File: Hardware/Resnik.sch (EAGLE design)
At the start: 172 parts, among them IC1 ATMEGA644M, J1 CONN_82.54_SCREW, J3 CONN_82.54_SCREW, J4 CONN_42.54_SCREW, Q1 DMG3404, Q2 DMG3404, Q3 FDN360P, Q4 FDN360P, Q5 FDN360P, Q6 DMG3404, U1 TLV61220DBV, U10 SN74AUP1G04YFP, U11 SN74AUP2G86SOT833-1, U12 SN74AUP2G08DQE, U13 SN74AUP2G08DQE, U14 SN74AUP2G08DQE, U15 MIC2039MT, U16 MIC2039MT, U17 MIC2039MT, U18 MIC2039MT, U19 TPS22917DBV, U2 TPS62822DLC, U20 TPS22917DBV, U21 TXS0102DQM, U22 BME280, U23 FT231X-Q, U24 TPS22917DBV, U25 TXS0108RGY, U26 TXS0108RGY, U27 TXS0104RGY, U28 MCP4726A2SOT-23, U29 ADS1115, U3 TPS61032RSA, U30 ADS1115, U31 INA211DCK, U32 INA210DCK, U33 TCA9555RTW, U5 BQ2980RUG, U6 TPS2105, U7 LTC4412S6, U8 TPS79733, U9 SN74AUP1G04YFP

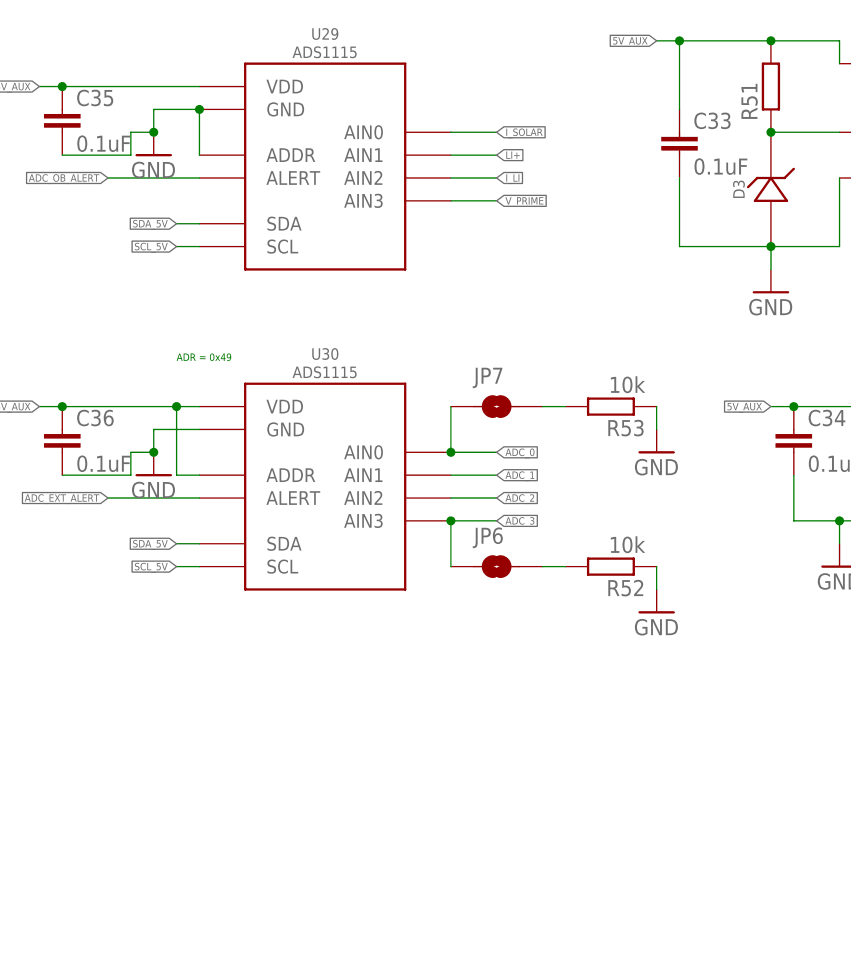
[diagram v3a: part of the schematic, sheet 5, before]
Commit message: Continued layout, major of power and prime bus done
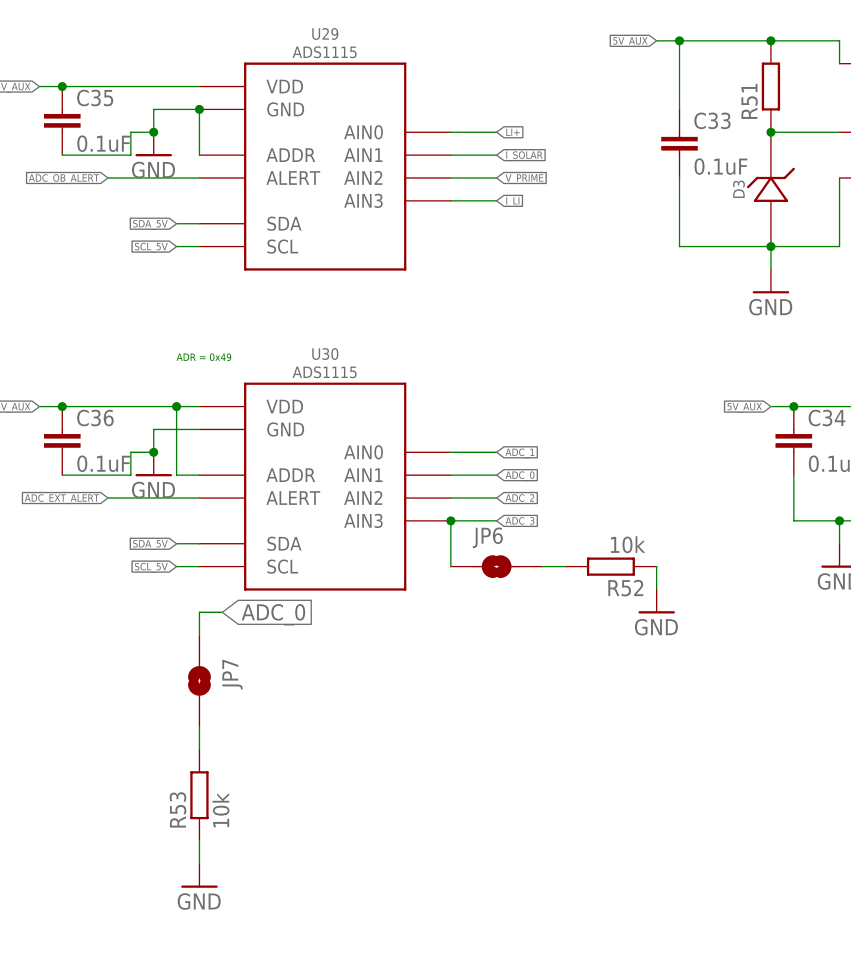
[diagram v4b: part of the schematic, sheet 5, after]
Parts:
- removed R22: 10k, bschulz_passives:R-EU_10KR0402
- added C37, C38, C39: (no value), bschulz_passives:C-EUC0402
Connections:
- net VBAT+ renamed V_CORE
- removed net 3V3: C25.1, IC1.AREF, IC1.AVCC, IC1.VCC, IC1.VCC@1, IC1.VCC@2, ISP2.VCC, R44.2, U$16.ANODE
- new net N$1: IC1.(PCINT2/ADC2)PA2
- net 3V3_AUX: now also C37.1, C38.1, C39.1
- net 3V3_CORE: now also C25.1, IC1.AREF, IC1.AVCC, IC1.VCC, IC1.VCC@1, IC1.VCC@2, ISP2.VCC, R44.2, U$16.ANODE; no longer R22.2
- net ADC_0: now also U30.AIN1; no longer U30.AIN0
- net ADC_1: now also U30.AIN0; no longer U30.AIN1
- net ADC_EXT_ALERT: now also U33.P7
- net BMS_CTR: now also U33.P1
- net BUS_LOGIC_EN_PRIME: now also U33.P6
- net FAULT_PRIME: now also U33.P5
- net GND: now also C37.2, C38.2, C39.2
- net GPIO_1: now also IC1.(PCINT1/ADC1)PA1
- net I_LI: now also U29.AIN3; no longer U29.AIN2
- net I_SOLAR: now also U29.AIN1; no longer U29.AIN0
- net LI+: now also U29.AIN0; no longer U29.AIN1
- net MPPT_CHRG: now also U33.P3
- net MPPT_FAULT: now also U33.P4
- net MPPT_SHDN: now also U33.P2
- net PG_LDO: no longer R22.1
- net SDA: no longer U21.A1
- net SDA_OB: now also U21.A1
- net VUSB_POWER: now also U33.P0
- net V_PRIME: now also U29.AIN2; no longer U29.AIN3
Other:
- note added: "ADD: --MPPT, CHRG (Input) --MPPT, FAULT (Input) --MPPT, SHDN (Output) Feather PowerOn (Output) ADC, OnBoard, Alert/RDY (Input, Interrupt) ADC, OffBoard, Alert/RDY (Input, Interrupt) --Vusb (Input) LevelShifter, Primary Bus, EN (Output) LevelShifter, Secondary Bus, EN (Output) --BMS, CTR (Output) BusPowerSwitch, Primary Bus, Fault (Input) BusPowerSwitch, Secondary Bus, Fault (Input) HighPowerBoost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"
- note removed: "ADD: MPPT, CHRG (Input) MPPT, FAULT (Input) MPPT, SHDN (Output) Feather PowerOn (Output) ADC, OnBoard, Alert/RDY (Input, Interrupt) ADC, OffBoard, Alert/RDY (Input, Interrupt) Vusb (Input) LevelShifter, Primary Bus, EN (Output) LevelShifter, Secondary Bus, EN (Output) BMS, CTR (Output) BusPowerSwitch, Primary Bus, Fault (Input) BusPowerSwitch, Secondary Bus, Fault (Input) HighPowerBoost, LBO (Inp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"
- moved on the sheet: JP7, R53

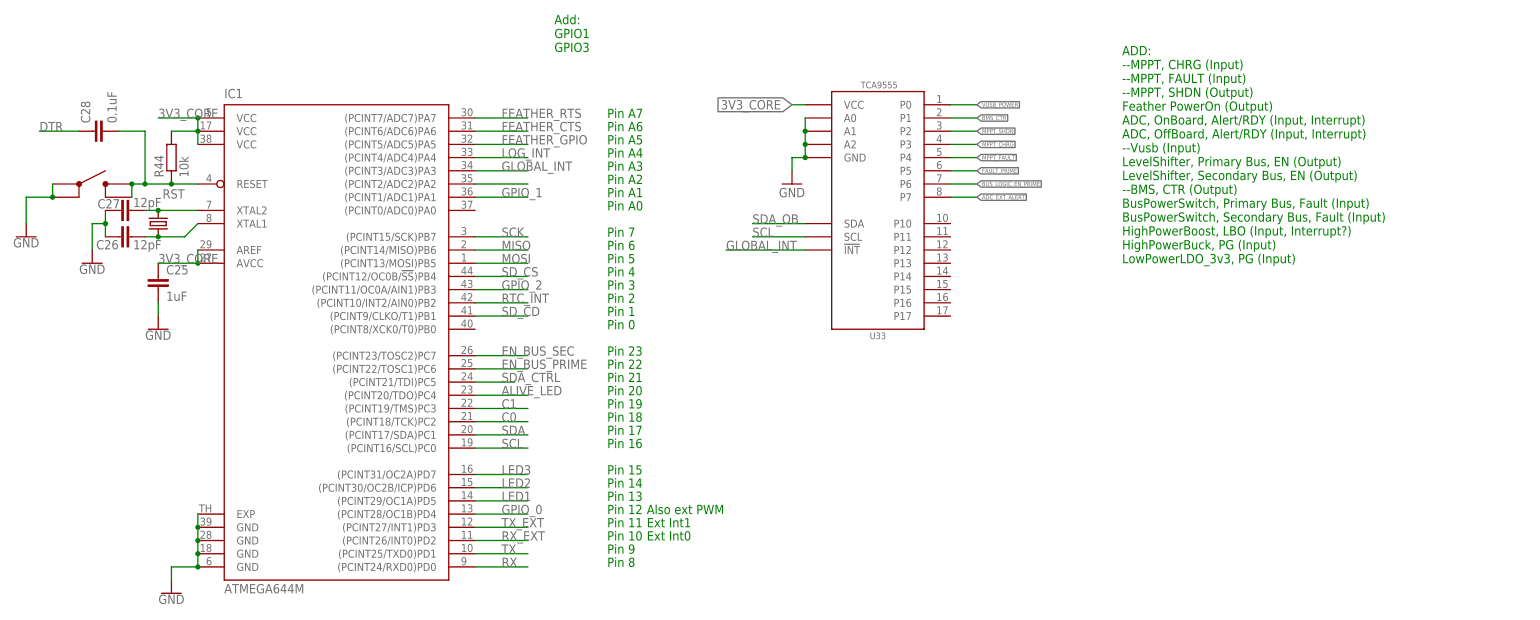
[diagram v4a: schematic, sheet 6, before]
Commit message: Continued layout, majority of secondary bus, low power
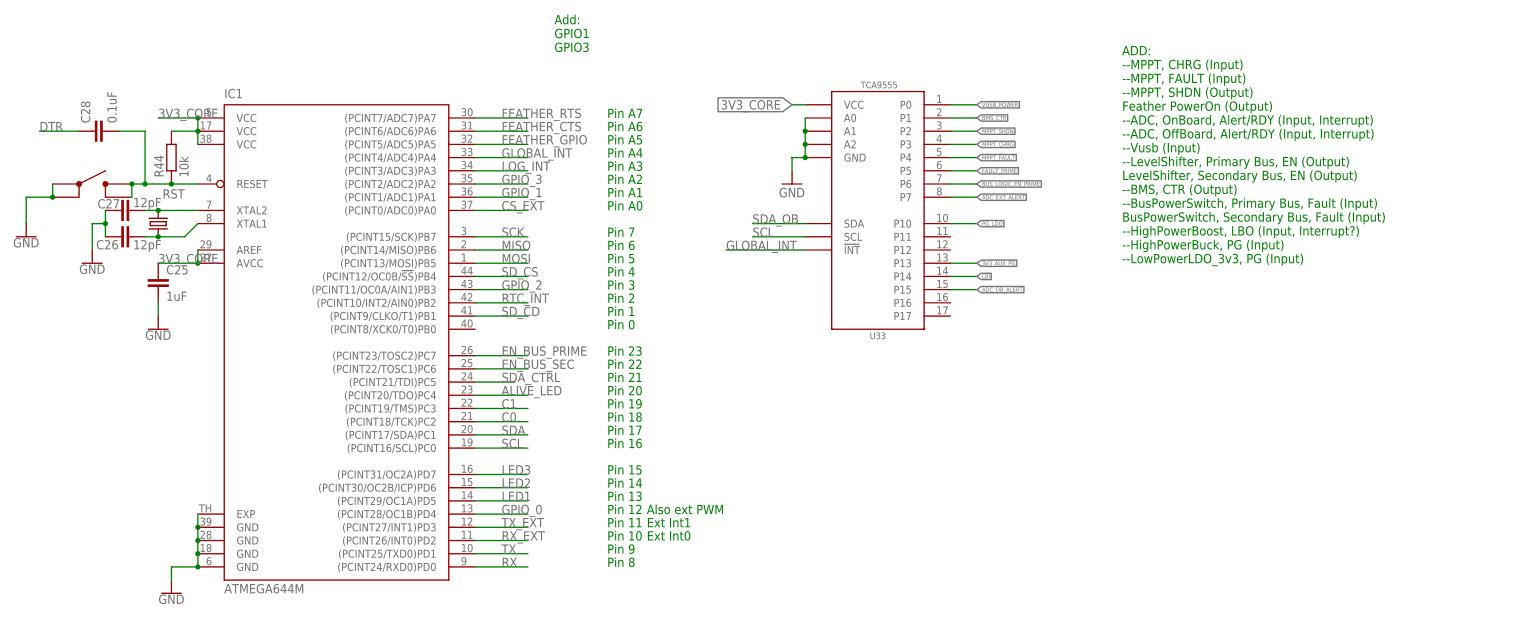
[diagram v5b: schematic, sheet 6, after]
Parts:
- added C40: (no value), bschulz_passives:C-EU0.1UFC0402
- added H1, H2, H3: (no value), bschulz:MOUNTING_HOLE4_NP
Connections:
- removed net N$1: IC1.(PCINT2/ADC2)PA2
- new net FAULT_SEC: U15.!FAULT, U16.!FAULT
- net 3V3_AUX_PG: now also U33.P13
- net ADC_OB_ALERT: now also U33.P15
- net CS_EXT: now also IC1.(PCINT0/ADC0)PA0
- net EN_BUS_PRIME: now also IC1.(PCINT23/TOSC2)PC7; no longer IC1.(PCINT22/TOSC1)PC6
- net EN_BUS_SEC: now also IC1.(PCINT22/TOSC1)PC6; no longer IC1.(PCINT23/TOSC2)PC7
- net FAULT_PRIME: no longer U15.!FAULT, U16.!FAULT
- net GLOBAL_INT: now also IC1.(PCINT4/ADC4)PA4; no longer IC1.(PCINT3/ADC3)PA3
- net GND: now also C40.2
- net GPIO_3: now also IC1.(PCINT2/ADC2)PA2
- net LBI: now also U33.P14
- net LOG_INT: now also IC1.(PCINT3/ADC3)PA3; no longer IC1.(PCINT4/ADC4)PA4
- net N$43: now also C40.1
- net PG_LDO: now also U33.P10
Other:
- note added: "ADD: --MPPT, CHRG (Input) --MPPT, FAULT (Input) --MPPT, SHDN (Output) Feather PowerOn (Output) --ADC, OnBoard, Alert/RDY (Input, Interrupt) --ADC, OffBoard, Alert/RDY (Input, Interrupt) --Vusb (Input) --LevelShifter, Primary Bus, EN (Output) LevelShifter, Secondary Bus, EN (Output) --BMS, CTR (Output) --BusPowerSwitch, Primary Bus, Fault (Input) BusPowerSwitch, Secondary Bus, Fault (Input) --High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"
- note removed: "ADD: --MPPT, CHRG (Input) --MPPT, FAULT (Input) --MPPT, SHDN (Output) Feather PowerOn (Output) ADC, OnBoard, Alert/RDY (Input, Interrupt) ADC, OffBoard, Alert/RDY (Input, Interrupt) --Vusb (Input) LevelShifter, Primary Bus, EN (Output) LevelShifter, Secondary Bus, EN (Output) --BMS, CTR (Output) BusPowerSwitch, Primary Bus, Fault (Input) BusPowerSwitch, Secondary Bus, Fault (Input) HighPowerBoost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"
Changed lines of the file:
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@@
 <part name="C39" library="bschulz_passives" deviceset="C-EU" device="C0402"/>
 <part name="GND67" library="supply1" library_urn="urn:adsk.eagle:library:371" deviceset="GND" device=""/>
+<part name="C40" library="bschulz_passives" deviceset="C-EU" device="C0402" technology="0.1UF"/>
+<part name="H1" library="bschulz" deviceset="MOUNTING_HOLE" device="4_NP"/>
+<part name="H2" library="bschulz" deviceset="MOUNTING_HOLE" device="4_NP"/>
+<part name="H3" library="bschulz" deviceset="MOUNTING_HOLE" device="4_NP"/>
 </parts>
 <sheets>
@@
 <label x="53.34" y="101.6" size="1.778" layer="95" xref="yes"/>
 </segment>
-<segment>
-<pinref part="U15" gate="G$1" pin="!FAULT"/>
-<pinref part="U16" gate="G$1" pin="!FAULT"/>
-<wire x1="48.26" y1="167.64" x2="48.26" y2="160.02" width="0.1524" layer="91"/>
-<wire x1="48.26" y1="160.02" x2="48.26" y2="152.4" width="0.1524" layer="91"/>
-<wire x1="48.26" y1="160.02" x2="53.34" y2="160.02" width="0.1524" layer="91"/>
-<junction x="48.26" y="160.02"/>
-<label x="53.34" y="160.02" size="1.778" layer="95" xref="yes"/>
-</segment>
 </net>
 <net name="N$27" class="0">
@@
 </segment>
 </net>
+<net name="FAULT_SEC" class="0">
+<segment>
+<pinref part="U15" gate="G$1" pin="!FAULT"/>
+<pinref part="U16" gate="G$1" pin="!FAULT"/>
+<wire x1="48.26" y1="167.64" x2="48.26" y2="160.02" width="0.1524" layer="91"/>
+<wire x1="48.26" y1="160.02" x2="48.26" y2="152.4" width="0.1524" layer="91"/>
+<wire x1="48.26" y1="160.02" x2="53.34" y2="160.02" width="0.1524" layer="91"/>
+<junction x="48.26" y="160.02"/>
+<label x="53.34" y="160.02" size="1.778" layer="95" xref="yes"/>
+</segment>
+</net>
 </nets>
 </sheet>
@@
 <instance part="J7" gate="G$1" x="205.74" y="73.66"/>
 <instance part="J8" gate="G$1" x="241.3" y="86.36" rot="R90"/>
+<instance part="H1" gate="G$1" x="114.3" y="10.16"/>
+<instance part="H2" gate="G$1" x="121.92" y="10.16"/>
+<instance part="H3" gate="G$1" x="129.54" y="10.16"/>
 </instances>
 <busses>
@@
 <instance part="GND60" gate="1" x="111.76" y="17.78"/>
 <instance part="GND61" gate="1" x="162.56" y="48.26"/>
+<instance part="C40" gate="G$1" x="68.58" y="27.94"/>
 </instances>
 <busses>
@@
 <pinref part="BT1" gate="G$1" pin="-"/>
 <wire x1="60.96" y1="20.32" x2="60.96" y2="22.86" width="0.1524" layer="91"/>
+<pinref part="C40" gate="G$1" pin="2"/>
+<wire x1="68.58" y1="22.86" x2="60.96" y2="22.86" width="0.1524" layer="91"/>
+<junction x="60.96" y="22.86"/>
 </segment>
 <segment>
@@
 <pinref part="BT1" gate="G$1" pin="+"/>
 <junction x="60.96" y="30.48"/>
+<pinref part="C40" gate="G$1" pin="1"/>
+<wire x1="68.58" y1="30.48" x2="60.96" y2="30.48" width="0.1524" layer="91"/>
 </segment>
 </net>
@@
 --MPPT, SHDN (Output)
 Feather PowerOn (Output)
-ADC, OnBoard, Alert/RDY (Input, Interrupt)
-ADC, OffBoard, Alert/RDY (Input, Interrupt)
+--ADC, OnBoard, Alert/RDY (Input, Interrupt)
+--ADC, OffBoard, Alert/RDY (Input, Interrupt)
 --Vusb (Input)
-LevelShifter, Primary Bus, EN (Output)
+--LevelShifter, Primary Bus, EN (Output)
 LevelShifter, Secondary Bus, EN (Output)
 --BMS, CTR (Output)
-BusPowerSwitch, Primary Bus, Fault (Input)
+--BusPowerSwitch, Primary Bus, Fault (Input)
 BusPowerSwitch, Secondary Bus, Fault (Input)
-HighPowerBoost, LBO (Input, Interrupt?)
-HighPowerBuck, PG (Input)
-LowPowerLDO_3v3, PG (Input)</text>
+--HighPowerBoost, LBO (Input, Interrupt?)
+--HighPowerBuck, PG (Input)
+--LowPowerLDO_3v3, PG (Input)</text>
 </plain>
 <instances>
@@
 <net name="EN_BUS_PRIME" class="0">
 <segment>
-<pinref part="IC1" gate="G$1" pin="(PCINT22/TOSC1)PC6"/>
-<wire x1="91.44" y1="55.88" x2="101.6" y2="55.88" width="0.1524" layer="91"/>
-<label x="96.52" y="55.88" size="1.778" layer="95"/>
-</segment>
-</net>
-<net name="EN_BUS_SEC" class="0">
-<segment>
 <pinref part="IC1" gate="G$1" pin="(PCINT23/TOSC2)PC7"/>
 <wire x1="91.44" y1="58.42" x2="101.6" y2="58.42" width="0.1524" layer="91"/>
@@
 <net name="LOG_INT" class="0">
 <segment>
-<pinref part="IC1" gate="G$1" pin="(PCINT4/ADC4)PA4"/>
-<wire x1="91.44" y1="96.52" x2="101.6" y2="96.52" width="0.1524" layer="91"/>
-<label x="96.52" y="96.52" size="1.778" layer="95"/>
+<pinref part="IC1" gate="G$1" pin="(PCINT3/ADC3)PA3"/>
+<wire x1="91.44" y1="93.98" x2="101.6" y2="93.98" width="0.1524" layer="91"/>
+<label x="96.52" y="93.98" size="1.778" layer="95"/>
 </segment>
 </net>
@@
 <net name="GLOBAL_INT" class="0">
 <segment>
-<pinref part="IC1" gate="G$1" pin="(PCINT3/ADC3)PA3"/>
-<wire x1="91.44" y1="93.98" x2="101.6" y2="93.98" width="0.1524" layer="91"/>
-<label x="96.52" y="93.98" size="1.778" layer="95"/>
-</segment>
-<segment>
 <pinref part="U33" gate="G$1" pin="!INT"/>
 <wire x1="154.94" y1="78.74" x2="139.7" y2="78.74" width="0.1524" layer="91"/>
 <label x="139.7" y="78.74" size="1.778" layer="95"/>
 </segment>
+<segment>
+<pinref part="IC1" gate="G$1" pin="(PCINT4/ADC4)PA4"/>
+<wire x1="91.44" y1="96.52" x2="101.6" y2="96.52" width="0.1524" layer="91"/>
+<label x="96.52" y="96.52" size="1.778" layer="95"/>
+</segment>
 </net>
 <net name="SDA_OB" class="0">
@@
 </segment>
 </net>
-<net name="N$1" class="0">
+<net name="GPIO_3" class="0">
 <segment>
 <pinref part="IC1" gate="G$1" pin="(PCINT2/ADC2)PA2"/>
 <wire x1="91.44" y1="91.44" x2="101.6" y2="91.44" width="0.1524" layer="91"/>
+<label x="96.52" y="91.44" size="1.778" layer="95"/>
 </segment>
 </net>
@@
 </segment>
 </net>
+<net name="CS_EXT" class="0">
+<segment>
+<pinref part="IC1" gate="G$1" pin="(PCINT0/ADC0)PA0"/>
+<wire x1="91.44" y1="86.36" x2="101.6" y2="86.36" width="0.1524" layer="91"/>
+<label x="96.52" y="86.36" size="1.778" layer="95"/>
+</segment>
+</net>
+<net name="EN_BUS_SEC" class="0">
+<segment>
+<pinref part="IC1" gate="G$1" pin="(PCINT22/TOSC1)PC6"/>
+<wire x1="91.44" y1="55.88" x2="101.6" y2="55.88" width="0.1524" layer="91"/>
+<label x="96.52" y="55.88" size="1.778" layer="95"/>
+</segment>
+</net>
+<net name="PG_LDO" class="0">
+<segment>
+<pinref part="U33" gate="G$1" pin="P10"/>
+<wire x1="182.88" y1="83.82" x2="187.96" y2="83.82" width="0.1524" layer="91"/>
+<label x="187.96" y="83.82" size="0.8128" layer="95" xref="yes"/>
+</segment>
+</net>
+<net name="3V3_AUX_PG" class="0">
+<segment>
+<pinref part="U33" gate="G$1" pin="P13"/>
+<wire x1="182.88" y1="76.2" x2="187.96" y2="76.2" width="0.1524" layer="91"/>
+<label x="187.96" y="76.2" size="0.8128" layer="95" xref="yes"/>
+</segment>
+</net>
+<net name="LBI" class="0">
+<segment>
+<pinref part="U33" gate="G$1" pin="P14"/>
+<wire x1="182.88" y1="73.66" x2="187.96" y2="73.66" width="0.1524" layer="91"/>
+<label x="187.96" y="73.66" size="0.8128" layer="95" xref="yes"/>
+</segment>
+</net>
+<net name="ADC_OB_ALERT" class="0">
+<segment>
+<pinref part="U33" gate="G$1" pin="P15"/>
+<wire x1="182.88" y1="71.12" x2="187.96" y2="71.12" width="0.1524" layer="91"/>
+<label x="187.96" y="71.12" size="0.8128" layer="95" xref="yes"/>
+</segment>
+</net>
